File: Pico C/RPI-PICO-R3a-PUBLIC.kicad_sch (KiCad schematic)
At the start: 38 parts, among them J3 USB_C_Receptacle_USB2.0_16P, J4 SM03B-SRSS-TB, Q1 DMG1012T-7, SW1 PTS810 SJM 250 SMTR LFSPTS810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, U2 RT6150B-33GQW, U3 W25Q16JVUXIQ, X1 ECS-120-8-33-JGN-TR

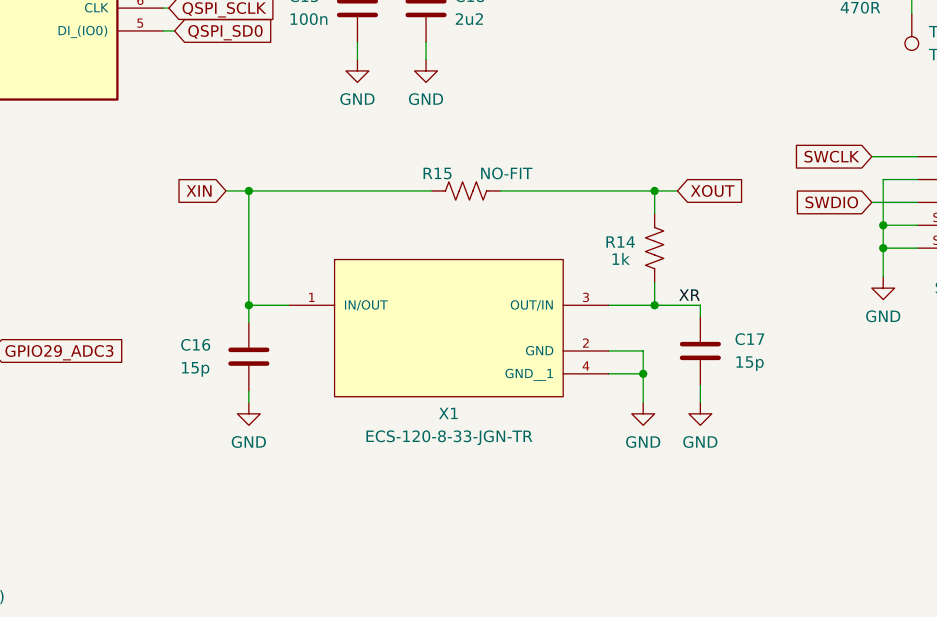
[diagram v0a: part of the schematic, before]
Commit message: Updated schematic for crystal
Updated the schematic symbol for the 12MHz crystal to be a KiCad included symbol.
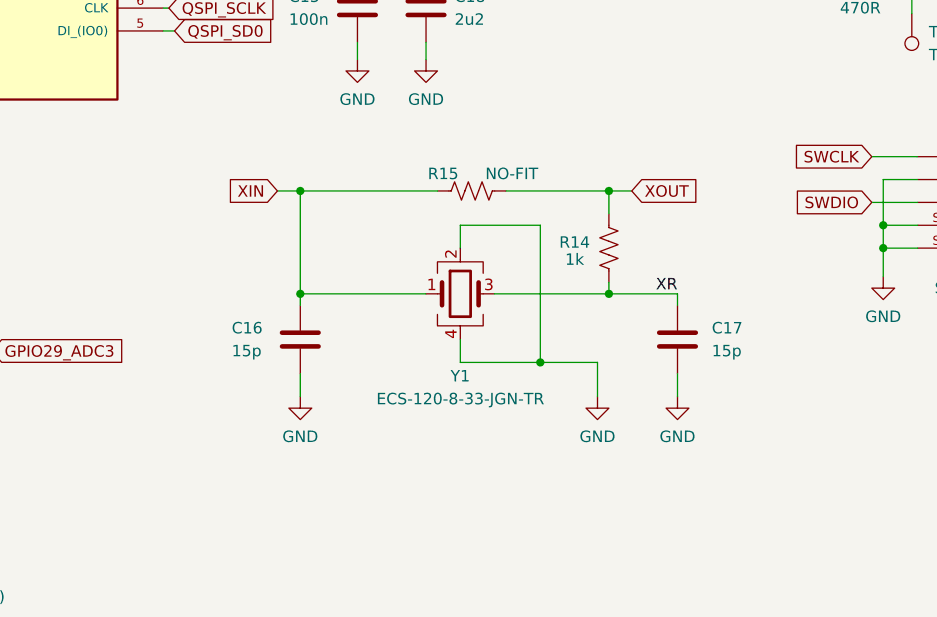
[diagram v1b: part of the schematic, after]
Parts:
- removed X1: ECS-120-8-33-JGN-TR, Pico_C:XTAL_ECS-120-8-33-JGN-TR, symbol Pico_C:ECS-120-8-33-JGN-TR
- added Y1: ECS-120-8-33-JGN-TR, Pico_C:XTAL_ECS-120-8-33-JGN-TR, symbol Device:Crystal_GND24
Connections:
- net GND: now also Y1.2, Y1.4
- net XIN: now also Y1.1
- net XR: now also Y1.3
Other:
- moved on the sheet: C16, C17, R14, R15
